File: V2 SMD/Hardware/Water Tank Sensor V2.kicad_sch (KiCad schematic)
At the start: 24 parts, among them J1 Valve Terminal, J2 Temp Sensor, J3 Water Level Sensor, J4 12v in, Q1 AO3400A, U1 ESP32-WROOM-32D, U2 AMS1117-3.3

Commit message: Added schematic image
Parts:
- added D3: Red LED, LED_SMD:LED_0805_2012Metric, symbol Device:LED_Small
- added D?: D_Schottky_Small, symbol Device:D_Schottky_Small
- added J?: Programming Header, symbol Connector:Conn_01x04_Male
- added R7: 2k, Resistor_SMD:R_0805_2012Metric, symbol Device:R_Small
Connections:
- net +12V: now also J4.2 (Pin_2); no longer J4.1 (Pin_1)
- net GND: now also J4.1 (Pin_1), J?.2 (Pin_2); no longer J4.2 (Pin_2)
- net RX-ESP: now also J?.4 (Pin_4)
- net TX-ESP: now also J?.3 (Pin_3)
- net VDD33: now also D?.1 (K)
- net at D1.2 (A), Relay1.2: now also R7.1; no longer Q1.3 (D)
- new net: D3.1 (K), Q1.3 (D)
- new net: D3.2 (A), R7.2
- new net: D?.2 (A), J?.1 (Pin_1)
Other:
- moved on the sheet: D1, J2, J3, Q1, R1, R2, R3, R4, Relay1

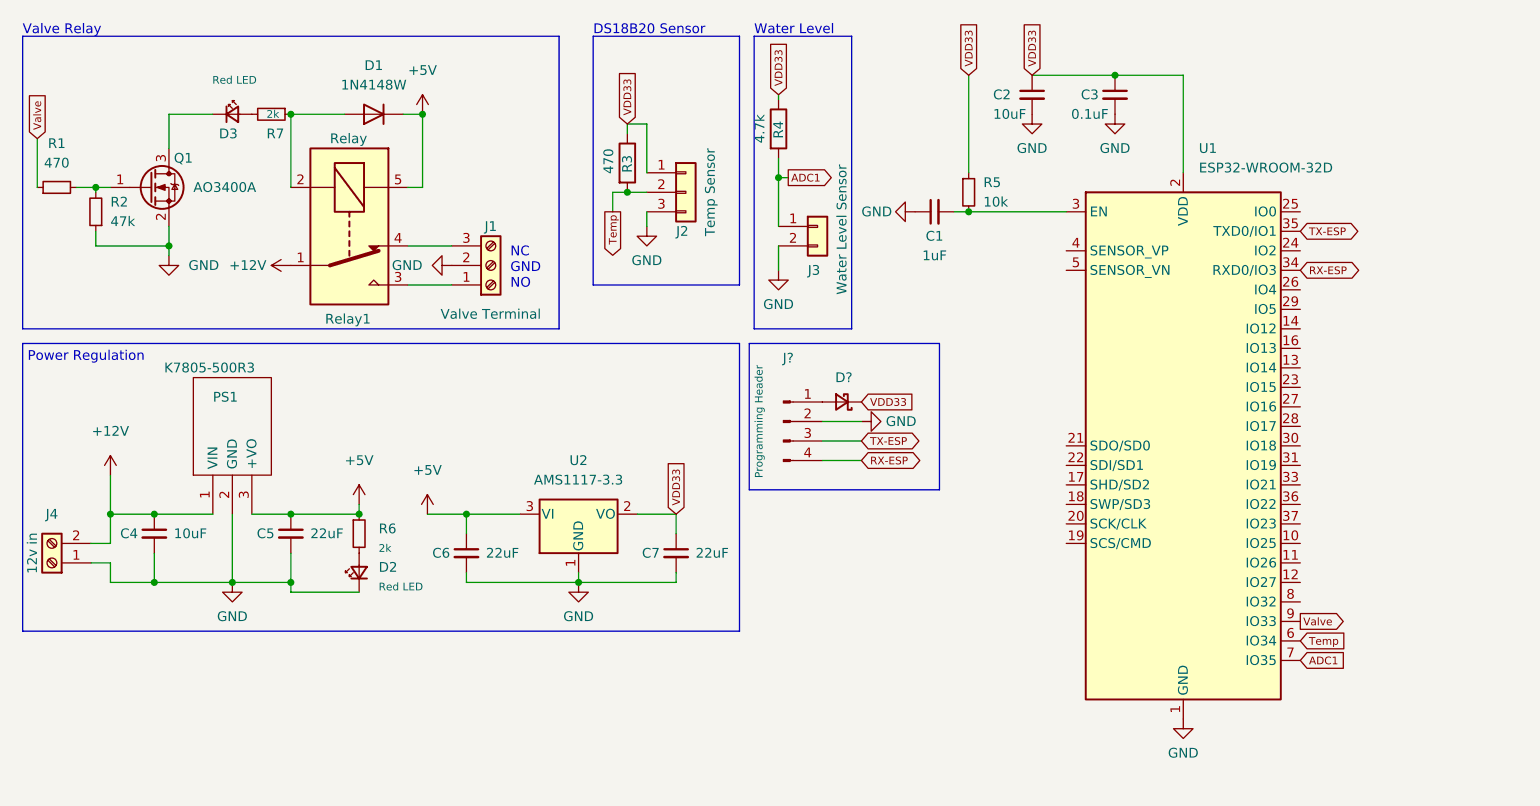
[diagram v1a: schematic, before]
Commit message: Added completed PCB layout for V2SMD with images
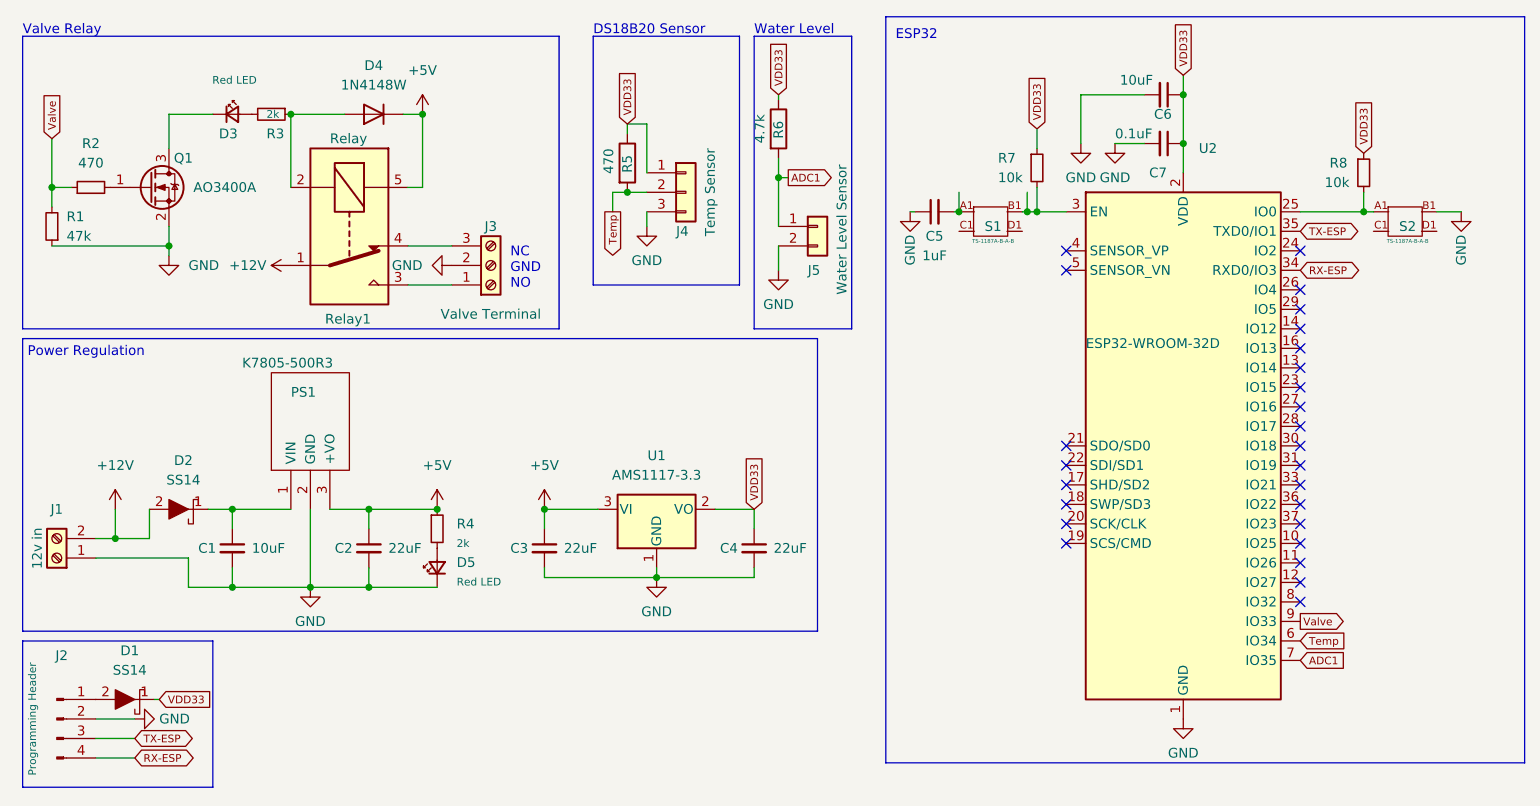
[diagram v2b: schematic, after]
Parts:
- removed D?: D_Schottky_Small, symbol Device:D_Schottky_Small
- removed R2: 47k, Resistor_SMD:R_0805_2012Metric, symbol Device:R_Small
- added D1, D2: SS14, SamacSys_Parts:DIOM5126X250N, symbol SamacSys_Parts:SS14
- added R1: 47k, Resistor_SMD:R_0805_2012Metric, symbol Device:R_Small
- added R8: 10k, Resistor_SMD:R_0805_2012Metric, symbol Device:R_Small
- added S1, S2: TS-1187A-B-A-B, SamacSys_Parts:TS1187ABAB, symbol TS-1187A-B-A-B:TS-1187A-B-A-B
- J2: renamed from J?; footprint (none) -> Connector_PinHeader_2.54mm:PinHeader_1x04_P2.54mm_Vertical
- J4: renamed from J2; footprint Connector_JST:JST_XH_B3B-XH-A_1x03_P2.50mm_Vertical -> Connector_JST:JST_XH_S3B-XH-A-1_1x03_P2.50mm_Horizontal
- J5: renamed from J3; footprint Connector_JST:JST_XH_B2B-XH-A_1x02_P2.50mm_Vertical -> Connector_JST:JST_XH_S2B-XH-A-1_1x02_P2.50mm_Horizontal
- renumbered C4 to C1, C5 to C2, C6 to C3, C7 to C4, C1 to C5, C2 to C6, C3 to C7, D1 to D4, D2 to D5, J4 to J1, J1 to J3, R1 to R2, R7 to R3, R6 to R4, R3 to R5, R4 to R6, R5 to R7, U2 to U1, U1 to U2
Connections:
- net +12V: now also D2.2; no longer C1.1, PS1.1 (VIN)
- net GND: now also R1.1, S2.B1
- net VDD33: now also D1.1, R8.1
- net Valve: now also R1.2
- net at J2.1 (Pin_1): now also D1.2
- net at U2.25 (IO0): now also R8.2, S2.A1
- net at R7.2, U2.3 (EN): now also S1.B1; no longer C5.2
- new net: C1.1, D2.1, PS1.1 (VIN)
- new net: C5.2, S1.A1
- no-connect marks 0 -> 26
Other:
- note added: "ESP32"
- moved on the sheet: C1, C2, C3, C4, C6, C7, D5, J1, J2, PS1, R2, R4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
